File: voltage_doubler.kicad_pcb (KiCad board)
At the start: 2 copper layers, 38.8 x 31.2 mm, 10 parts, among them IC1 LT1054CP, J1 Vin = 3.5V to 15V, J2 Barrel_Jack

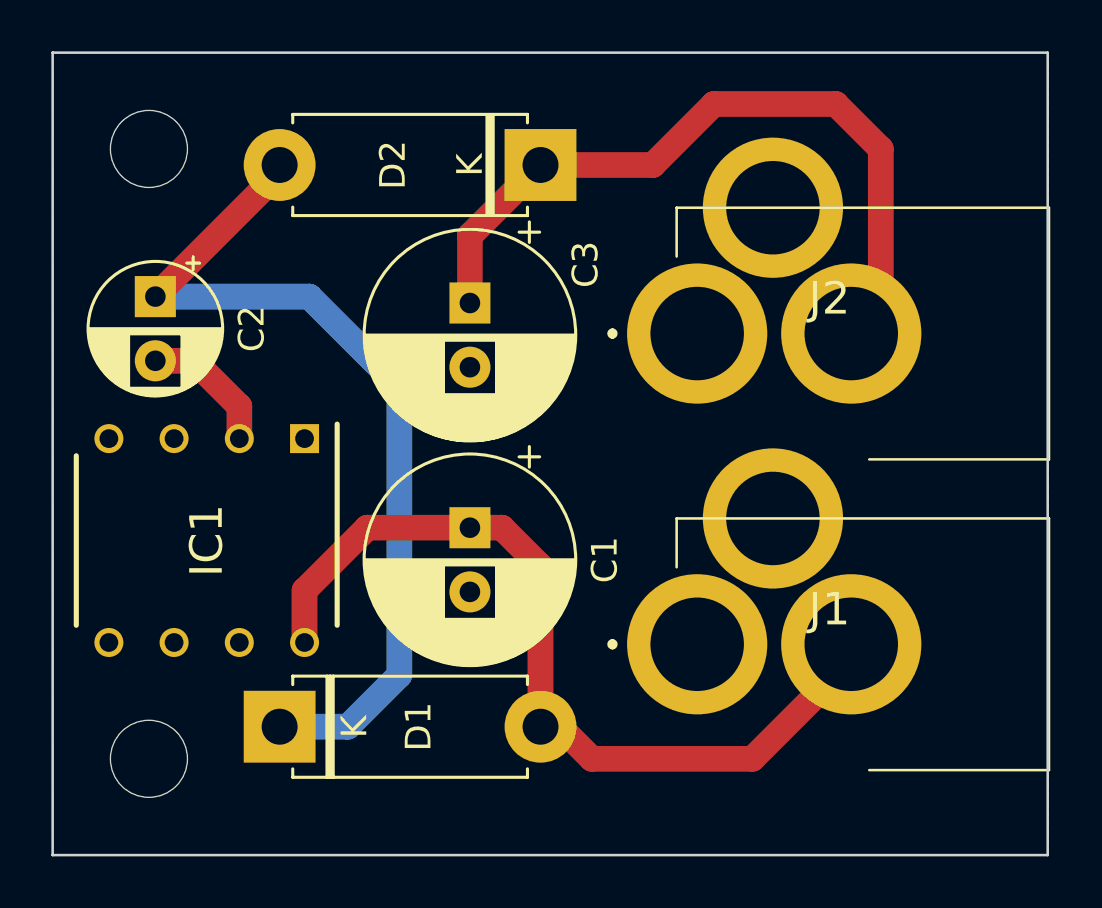
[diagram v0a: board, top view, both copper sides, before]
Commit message: update checklist, add graphics, add date variable
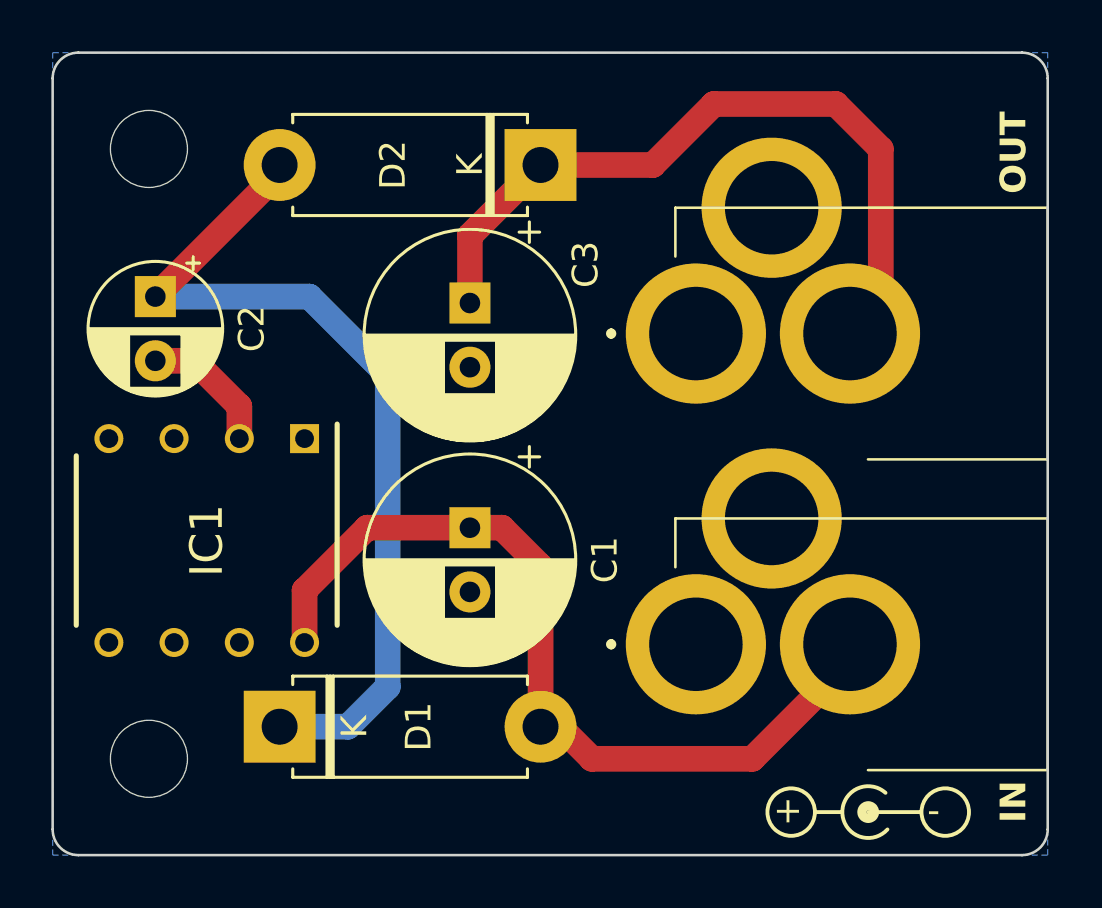
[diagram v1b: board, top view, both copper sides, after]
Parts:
- added REF**: Symbol_Barrel_Polarity, Symbol:Symbol_Barrel_Polarity, F.Cu at (153.5, 97.0)
- added REF**: Symbol_Barrel_Polarity, Symbol:Symbol_Barrel_Polarity, B.Cu at (157.0, 83.1)
- added REF**: KiCad-Logo2_5mm_SilkScreen, Symbol:KiCad-Logo2_5mm_SilkScreen, B.Cu at (130.2, 86.5)
- moved J1 0.05 mm to (151.9, 89.2)
- moved J2 0.05 mm to (151.9, 77.1)
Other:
- outline, holes or cut-outs redrawn
- board text added: "+"
- board text added: "-"
- board text added: "IN"
- board text added: "OUT"
- board text added: "milos.garunovic ${MANUFACTURING_DATE}"
